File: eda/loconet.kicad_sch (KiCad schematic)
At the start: 72 parts, among them J1 RJ12, J10 FROG4, J11 LN Debug, J12 LN Raw, J13 Input voltage, J14 IO, J15 Power, J2 DCC IN, J3 FROG1, J4 DCC1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

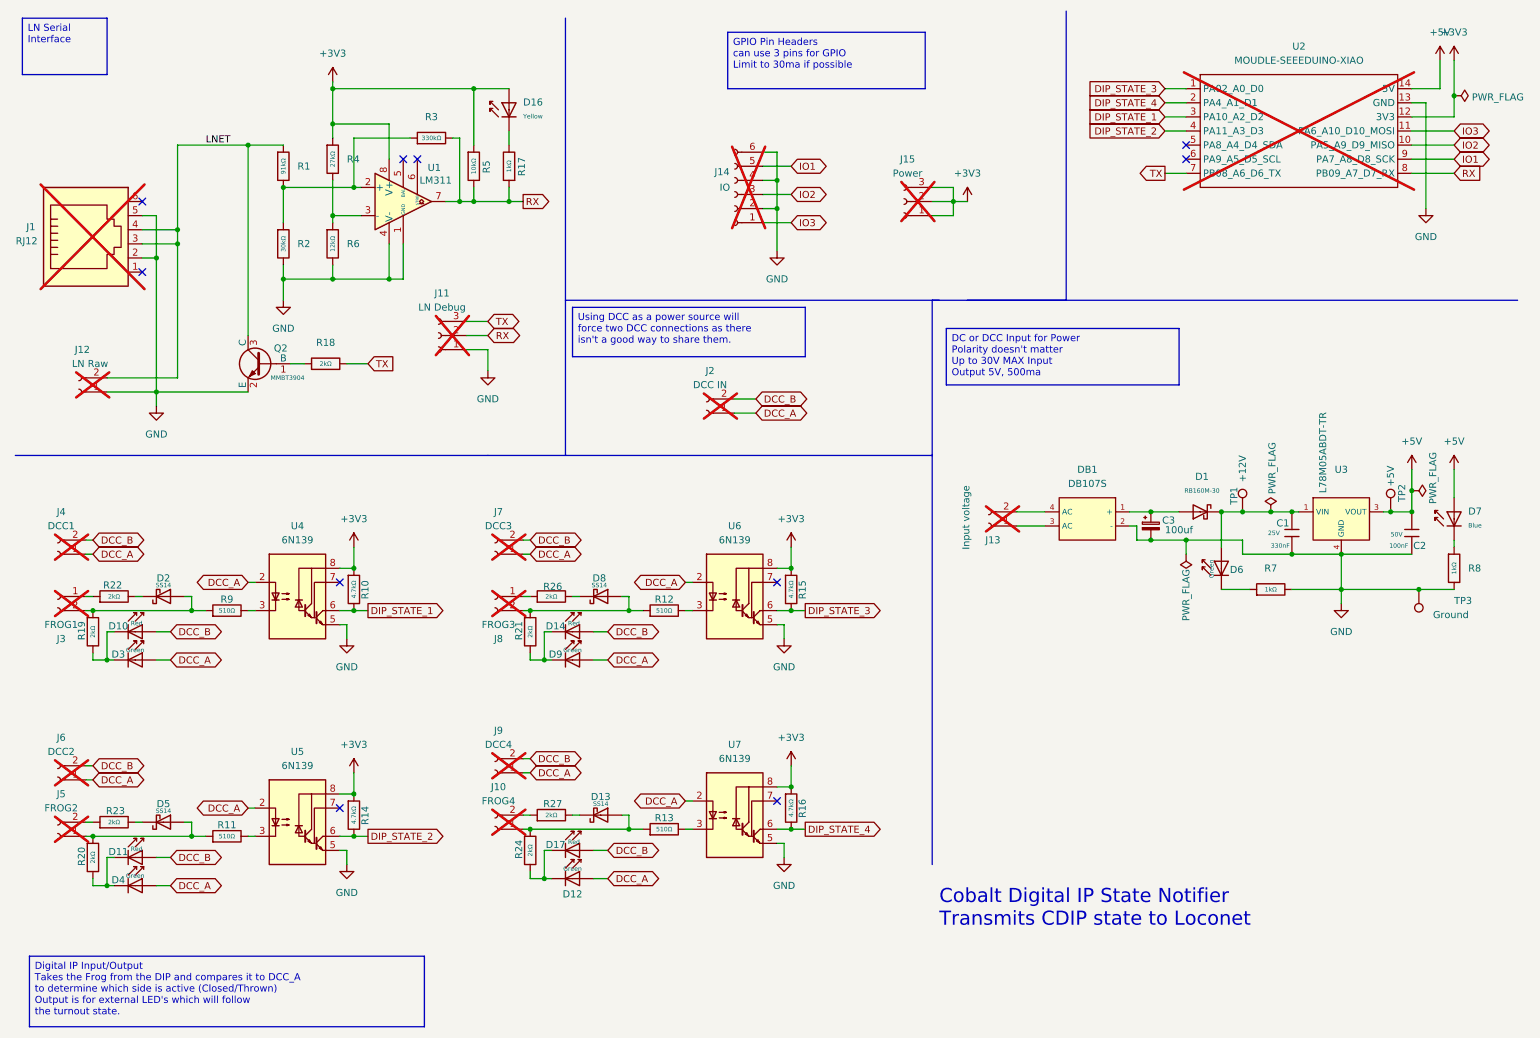
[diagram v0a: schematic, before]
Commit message: Mostly works now, but there is still at least one issue.
* PCB seems to work just fine for reading inputs, and can communicate with a DCS52
* Code has been tweaked a bit, and the inverted parameters are weird, but opposites work
* For whatever reason, when I plug in the USB to DCS52 and connect JMRI, this all goes to hell
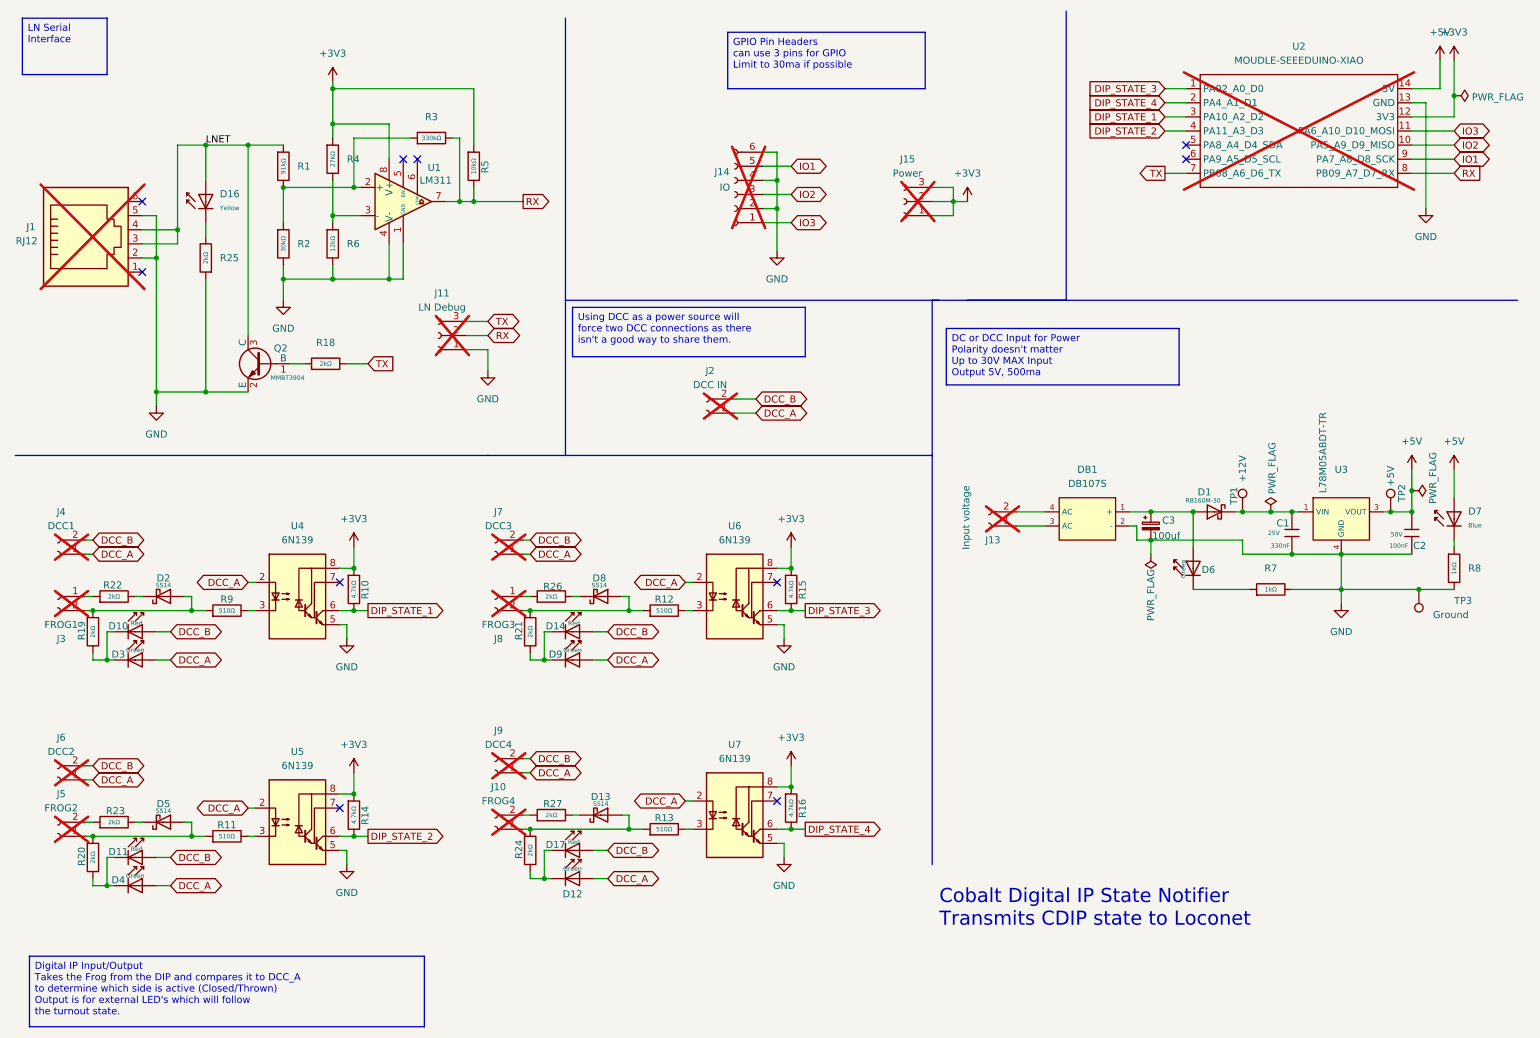
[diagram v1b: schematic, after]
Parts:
- removed J12: LN Raw, Connector_PinHeader_2.54mm:PinHeader_1x02_P2.54mm_Vertical, symbol Connector:Conn_01x02_Socket
- removed R17: 1kΩ, PCM_JLCPCB:R_0402, symbol PCM_JLCPCB-Resistors:0402,1kΩ
- added R25: 2kΩ, PCM_JLCPCB:R_0402, symbol PCM_JLCPCB-Resistors:0402,2kΩ
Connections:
- net +3V3: no longer D16.2
- net GND: now also R25.1
- net LNET: now also D16.2
- net at C1.1, D1.1, TP1.1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: no longer D6.2
- net at C3.1, D1.2, DB1.1 (+): now also D6.2
- net at D16.1: now also R25.2
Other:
- moved on the sheet: D1, D16, D6
